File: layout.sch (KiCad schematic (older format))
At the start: 20 parts

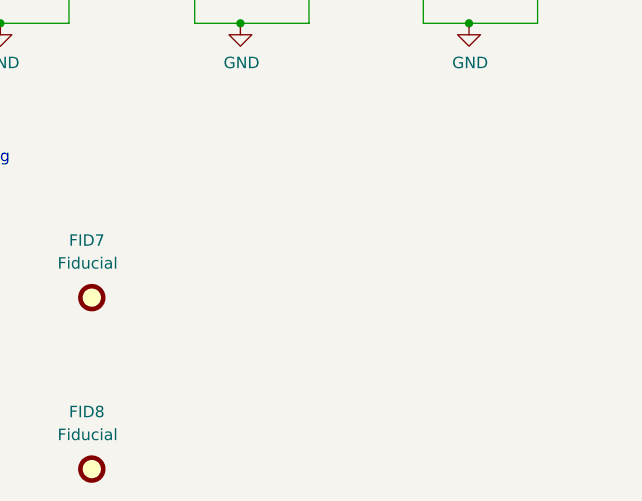
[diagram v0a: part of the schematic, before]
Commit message: Change R13 to a no-connection item
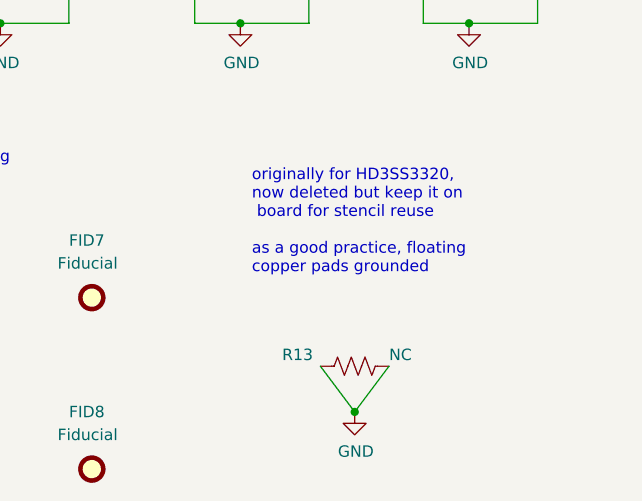
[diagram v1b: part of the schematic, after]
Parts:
- added R13: NC, Resistor_SMD:R_0603_1608Metric_Pad0.98x0.95mm_HandSolder, symbol Device:R_US
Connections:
- net GND: now also R13.1, R13.2
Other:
- note added: "originally for HD3SS3320,\nnow deleted but keep it on\n board for stencil reuse\n\nas a good practice, floating\ncopper pads grounded"
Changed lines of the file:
@@
 	1    0    0    -1
 $EndComp
+$Comp
+L power:GND #PWR0149
+U 1 1 60DACF23
+P 7800 5450
+F 0 "#PWR0149" H 7800 5200 50  0001 C CNN
+F 1 "GND" H 7805 5277 50  0000 C CNN
+F 2 "" H 7800 5450 50  0001 C CNN
+F 3 "" H 7800 5450 50  0001 C CNN
+	1    7800 5450
+	1    0    0    -1
+$EndComp
+Wire Wire Line
+	7650 5250 7800 5450
+Wire Wire Line
+	7950 5250 7800 5450
+Connection ~ 7800 5450
+Text Notes 7350 4850 0    50   ~ 0
+originally for HD3SS3320,\nnow deleted but keep it on\n board for stencil reuse\n\nas a good practice, floating\ncopper pads grounded
+$Comp
+L Device:R_US R?
+U 1 1 60D66ED8
+P 7800 5250
+AR Path="/60085564/60D66ED8" Ref="R?"  Part="1"
+AR Path="/60C6101E/60D66ED8" Ref="R13"  Part="1"
+F 0 "R13" V 7750 5000 50  0000 C CNN
+F 1 "NC" V 7750 5450 50  0000 C CNN
+F 2 "Resistor_SMD:R_0603_1608Metric_Pad0.98x0.95mm_HandSolder" V 7840 5240 50  0001 C CNN
+F 3 "~" H 7800 5250 50  0001 C CNN
+	1    7800 5250
+	0    1    1    0
+$EndComp
 $EndSCHEMATC

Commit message: various changes for v0.01 public release.
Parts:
- removed R13: NC, Resistor_SMD:R_0603_1608Metric_Pad0.98x0.95mm_HandSolder, symbol Device:R_US
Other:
- note removed: "originally for HD3SS3320,\nnow deleted but keep it on\n board for stencil reuse\n\nas a good practice, floating\ncopper pads grounded"
- moved on the sheet: C71, C72, C73, C74, C75, C76, C77, C78, C79, C80, C81, C82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

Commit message: v0.02.
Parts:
- added H1, H2, H3, H4: MountingHole_Pad, MountingHole:MountingHole_2.5mm_Pad_Via, symbol Mechanical:MountingHole_Pad
- added TP1, TP2, TP3: TestPoint, TestPoint:TestPoint_Pad_D1.0mm, symbol Connector:TestPoint
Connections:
- net +3V3: now also TP1.1
- net GND: now also H1.1, H2.1, H3.1, H4.1
- new net +1V2: TP3.1
- new net +1V5: TP2.1
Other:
- note added: "VL670: +1V5\nVL671: +1V2"
- moved on the sheet: C71, C72, C73, C74, C75, C76, C77, C78, C79, C80, C81, C82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
